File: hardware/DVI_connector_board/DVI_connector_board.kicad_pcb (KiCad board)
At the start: 2 copper layers, 19.8 x 22.9 mm, 7 parts, among them J1 FPC Cable connector 1x20, J2 HDMI_A

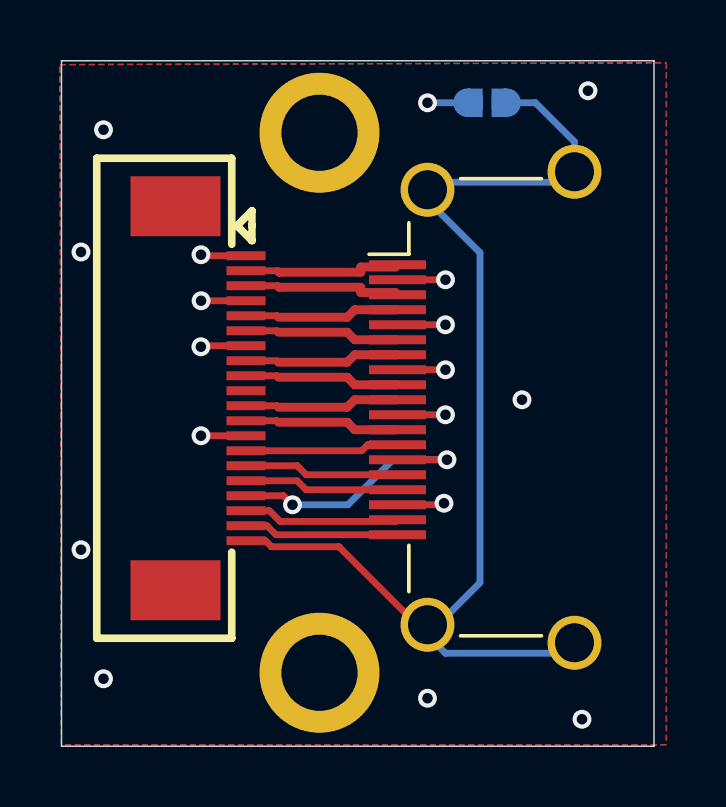
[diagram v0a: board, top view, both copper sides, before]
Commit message: Change pinout for being compatible with common extension cables
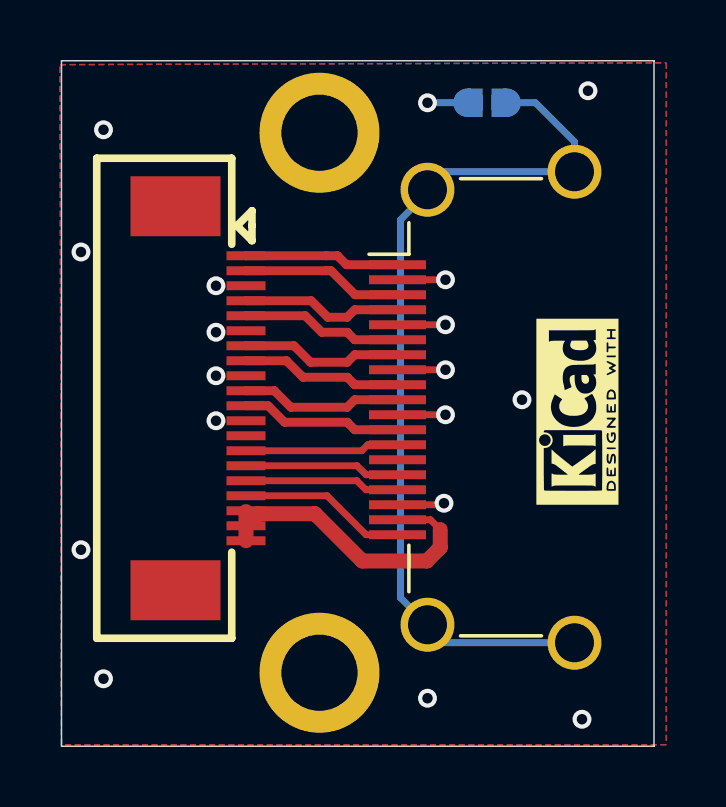
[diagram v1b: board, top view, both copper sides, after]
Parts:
- G***: moved to F.Cu
- moved G*** 9.00 mm to (122.8, 86.8)
- moved G*** 0.63 mm to (124.6, 87.3), turned to 90 degrees
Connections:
- J1 pad 1: GND -> /D2+
- J1 pad 10: GND -> /CK+
- J1 pad 11: /CK+ -> /CK-
- J1 pad 12: /CK- -> GND
- J1 pad 17: Net-(J2-UTILITY) -> Net-(J2-HPD)
- J1 pad 19: Net-(J2-HPD) -> Net-(J2-+5V)
- J1 pad 2: /D2+ -> /D2-
- J1 pad 20: Net-(JP1-B) -> Net-(J2-+5V)
- J1 pad 3: /D2- -> GND
- J1 pad 4: GND -> /D1+
- J1 pad 5: /D1+ -> /D1-
- J1 pad 6: /D1- -> GND
- J1 pad 7: GND -> /D0+
- J1 pad 8: /D0+ -> /D0-
- J1 pad 9: /D0- -> GND
- J2 pad 14: Net-(J2-UTILITY) -> unconnected-(J2-UTILITY-Pad14)
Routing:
- net Net-(J2-UTILITY): track 9.10 -> 0.00 mm, vias 2 -> 0
- net Net-(JP1-B): track 37.8 -> 29.4 mm
- net GND: track 15.6 -> 9.58 mm
- net Net-(J2-+5V): track 5.22 -> 10.6 mm
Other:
- board text added: "DVI Connector v0.1"
- board text added: "VERSION:"
- board text removed: "CERN OHL-S license"
- board text removed: "DVI Connector V0.09"

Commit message: review and update manufacturing constraints (via size, etc.)
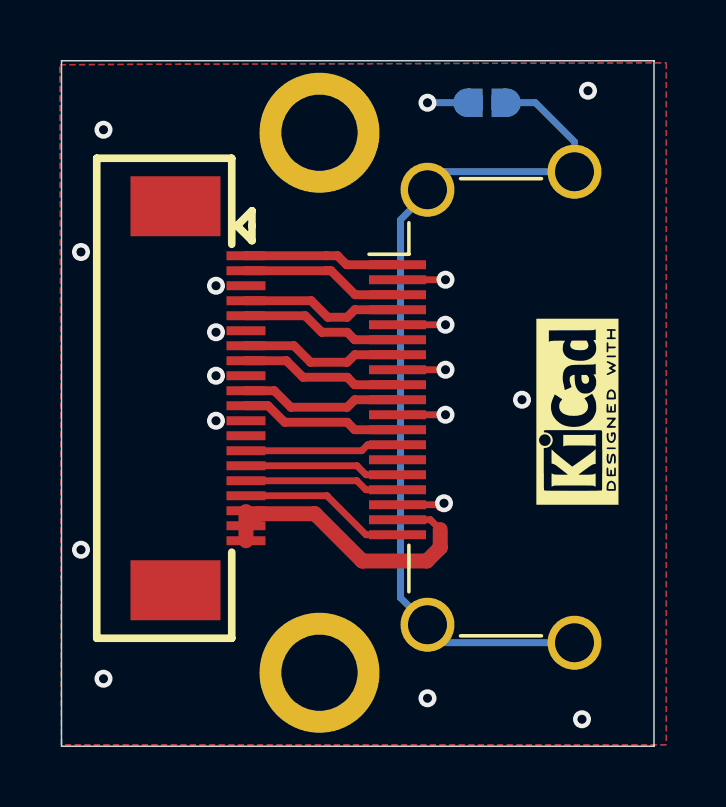
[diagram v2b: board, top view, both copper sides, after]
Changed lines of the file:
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@@
 		(at 124.596304 87.3 90)
 		(property "Reference" "G***"
-			(at 0 0 270)
+			(at 0 0 -90)
 			(layer "F.Fab")
 			(hide yes)
@@
 		)
 		(property "Value" "LOGO"
-			(at 0.75 0 270)
+			(at 0.75 0 -90)
 			(layer "F.Fab")
 			(hide yes)
@@
 	(via
 		(at 120.2 85.9)
-		(size 0.63)
-		(drill 0.35)
+		(size 0.6)
+		(drill 0.3)
 		(layers "F.Cu" "B.Cu")
 		(net 1)
@@
 	(via
 		(at 124.95 76.6)
-		(size 0.63)
-		(drill 0.35)
+		(size 0.6)
+		(drill 0.3)
 		(layers "F.Cu" "B.Cu")
 		(free yes)
@@
 	(via
 		(at 108.8 77.9)
-		(size 0.63)
-		(drill 0.35)
+		(size 0.6)
+		(drill 0.3)
 		(layers "F.Cu" "B.Cu")
 		(free yes)
@@
 	(via
 		(at 108.05 81.975)
-		(size 0.63)
-		(drill 0.35)
+		(size 0.6)
+		(drill 0.3)
 		(layers "F.Cu" "B.Cu")
 		(free yes)
@@
 	(via
 		(at 120.2 82.9)
-		(size 0.63)
-		(drill 0.35)
+		(size 0.6)
+		(drill 0.3)
 		(layers "F.Cu" "B.Cu")
 		(net 1)
@@
 	(via
 		(at 112.55 84.65)
-		(size 0.63)
-		(drill 0.35)
+		(size 0.6)
+		(drill 0.3)
 		(layers "F.Cu" "B.Cu")
 		(free yes)
@@
 	(via
 		(at 108.8 96.2)
-		(size 0.63)
-		(drill 0.35)
+		(size 0.6)
+		(drill 0.3)
 		(layers "F.Cu" "B.Cu")
 		(free yes)
@@
 	(via
 		(at 112.55 86.099622)
-		(size 0.63)
-		(drill 0.35)
+		(size 0.6)
+		(drill 0.3)
 		(layers "F.Cu" "B.Cu")
 		(free yes)
@@
 	(via
 		(at 120.15 90.35)
-		(size 0.63)
-		(drill 0.35)
+		(size 0.6)
+		(drill 0.3)
 		(layers "F.Cu" "B.Cu")
 		(free yes)
@@
 	(via
 		(at 112.55 87.6)
-		(size 0.63)
-		(drill 0.35)
+		(size 0.6)
+		(drill 0.3)
 		(layers "F.Cu" "B.Cu")
 		(free yes)
@@
 	(via
 		(at 120.2 84.4)
-		(size 0.63)
-		(drill 0.35)
+		(size 0.6)
+		(drill 0.3)
 		(layers "F.Cu" "B.Cu")
 		(net 1)
@@
 	(via
 		(at 108.05 91.9)
-		(size 0.63)
-		(drill 0.35)
+		(size 0.6)
+		(drill 0.3)
 		(layers "F.Cu" "B.Cu")
 		(free yes)
@@
 	(via
 		(at 124.75 97.55)
-		(size 0.63)
-		(drill 0.35)
+		(size 0.6)
+		(drill 0.3)
 		(layers "F.Cu" "B.Cu")
 		(free yes)
@@
 	(via
 		(at 120.2 87.4)
-		(size 0.63)
-		(drill 0.35)
+		(size 0.6)
+		(drill 0.3)
 		(layers "F.Cu" "B.Cu")
 		(net 1)
@@
 	(via
 		(at 112.55 83.1)
-		(size 0.63)
-		(drill 0.35)
+		(size 0.6)
+		(drill 0.3)
 		(layers "F.Cu" "B.Cu")
 		(free yes)
@@
 	(via
 		(at 119.6 77)
-		(size 0.63)
-		(drill 0.35)
+		(size 0.6)
+		(drill 0.3)
 		(layers "F.Cu" "B.Cu")
 		(free yes)
@@
 	(via
 		(at 122.75 86.9)
-		(size 0.63)
-		(drill 0.35)
+		(size 0.6)
+		(drill 0.3)
 		(layers "F.Cu" "B.Cu")
 		(free yes)
@@
 	(via
 		(at 119.6 96.85)
-		(size 0.63)
-		(drill 0.35)
+		(size 0.6)
+		(drill 0.3)
 		(layers "F.Cu" "B.Cu")
 		(free yes)
